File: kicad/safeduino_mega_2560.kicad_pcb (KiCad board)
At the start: 4 copper layers, 134.5 x 63.9 mm, 128 parts, among them X1 USB

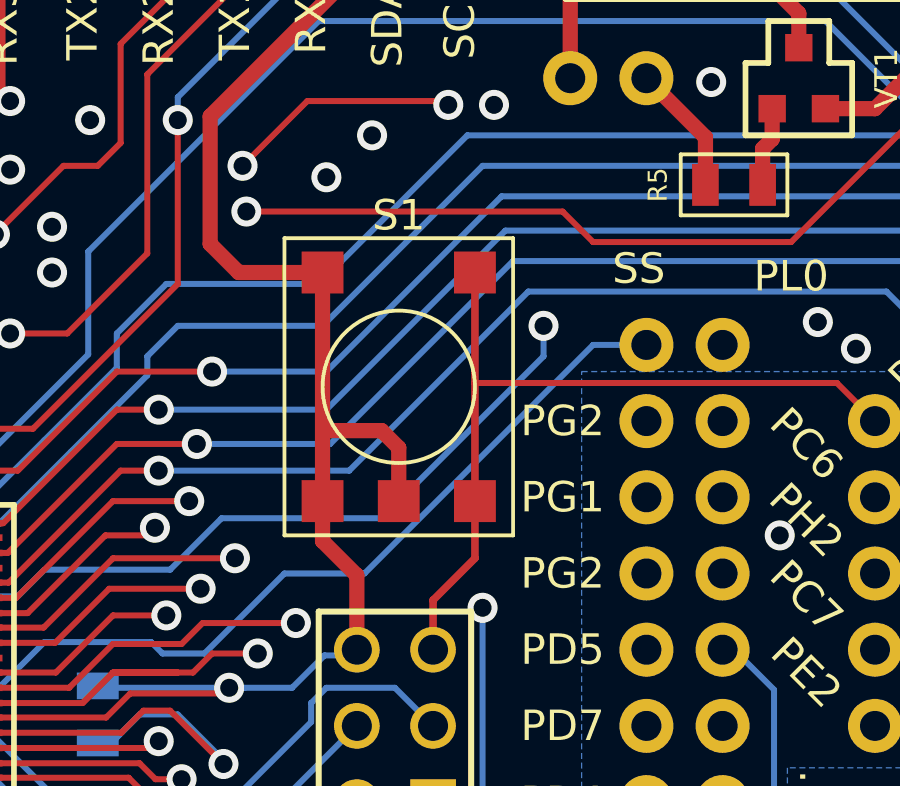
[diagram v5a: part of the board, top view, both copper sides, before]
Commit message: Поправил шелкографию и посадочное место для кнопки Reset.
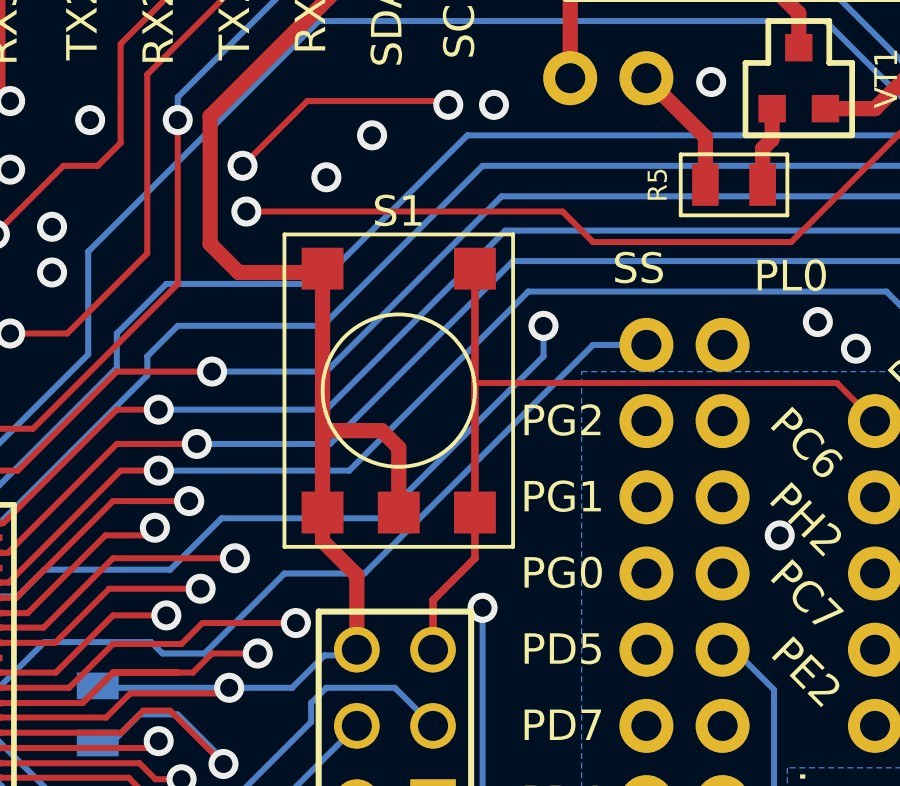
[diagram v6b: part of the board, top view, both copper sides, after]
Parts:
- moved S1 0.13 mm to (137.8, 114.3)
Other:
- board text added: "PG0"
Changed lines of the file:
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@@
     )
   )
-  (module SWD_BUTTON (layer Front)
-    (at 137.795 114.427 270)
-    (fp_text reference S1 (at -5.715 0 360) (layer F.SilkS)
-      (effects (font (size 1.016 1.016) (thickness 0.2032)))
-    )
-    (fp_text value DTSGL-61K (at 0.381 4.826 270) (layer F.SilkS) hide
-      (effects (font (size 1.016 1.016) (thickness 0.2032)))
-    )
-    (fp_line (start -4.953 3.81) (end 4.953 3.81) (layer F.SilkS) (width 0.127))
-    (fp_line (start -4.953 -3.81) (end 4.953 -3.81) (layer F.SilkS) (width 0.127))
-    (fp_circle (center 0 0) (end 0 -2.54) (layer F.SilkS) (width 0.127))
-    (fp_line (start 4.953 -3.81) (end 4.953 3.81) (layer F.SilkS) (width 0.127))
-    (fp_line (start -4.953 -3.81) (end -4.953 3.81) (layer F.SilkS) (width 0.127))
-    (pad 5 smd rect (at 3.81 0 270) (size 1.397 1.397)
-      (layers Front F.Paste F.Mask)
-      (net 21 /GND)
-    )
-    (pad 2 smd rect (at 3.81 -2.54 270) (size 1.397 1.397)
-      (layers Front F.Paste F.Mask)
-      (net 94 /RESET)
-    )
-    (pad 4 smd rect (at 3.81 2.54 270) (size 1.397 1.397)
-      (layers Front F.Paste F.Mask)
-      (net 21 /GND)
-    )
-    (pad 1 smd rect (at -3.81 -2.54 270) (size 1.397 1.397)
-      (layers Front F.Paste F.Mask)
-      (net 94 /RESET)
-    )
-    (pad 3 smd rect (at -3.81 2.54 270) (size 1.397 1.397)
-      (layers Front F.Paste F.Mask)
-      (net 21 /GND)
-    )
-  )
   (module CASE_C (layer Front)
     (at 75.692 124.206 180)
@@
     )
   )
+  (module SWD_BUTTON (layer Front)
+    (at 137.795 114.3 270)
+    (fp_text reference S1 (at -5.715 0 360) (layer F.SilkS)
+      (effects (font (size 1.016 1.016) (thickness 0.2032)))
+    )
+    (fp_text value DTSGL-61K (at 0.381 4.826 270) (layer F.SilkS) hide
+      (effects (font (size 1.016 1.016) (thickness 0.2032)))
+    )
+    (fp_line (start -4.953 3.81) (end 5.461 3.81) (layer F.SilkS) (width 0.127))
+    (fp_line (start -4.953 -3.81) (end 5.461 -3.81) (layer F.SilkS) (width 0.127))
+    (fp_circle (center 0.254 0) (end 0.254 -2.54) (layer F.SilkS) (width 0.127))
+    (fp_line (start 5.461 -3.81) (end 5.461 3.81) (layer F.SilkS) (width 0.127))
+    (fp_line (start -4.953 -3.81) (end -4.953 3.81) (layer F.SilkS) (width 0.127))
+    (pad 5 smd rect (at 4.318 0 270) (size 1.397 1.397)
+      (layers Front F.Paste F.Mask)
+      (net 21 /GND)
+    )
+    (pad 2 smd rect (at 4.318 -2.54 270) (size 1.397 1.397)
+      (layers Front F.Paste F.Mask)
+      (net 94 /RESET)
+    )
+    (pad 4 smd rect (at 4.318 2.54 270) (size 1.397 1.397)
+      (layers Front F.Paste F.Mask)
+      (net 21 /GND)
+    )
+    (pad 1 smd rect (at -3.81 -2.54 270) (size 1.397 1.397)
+      (layers Front F.Paste F.Mask)
+      (net 94 /RESET)
+    )
+    (pad 3 smd rect (at -3.81 2.54 270) (size 1.397 1.397)
+      (layers Front F.Paste F.Mask)
+      (net 21 /GND)
+    )
+  )
   (gr_text GND (at 155.448 151.765) (layer F.SilkS)
     (effects (font (size 1.016 1.016) (thickness 0.127)))
@@
     (effects (font (size 1.016 1.016) (thickness 0.127)))
   )
-  (gr_text PG2 (at 143.256 120.65) (layer F.SilkS)
+  (gr_text PG0 (at 143.256 120.65) (layer F.SilkS)
     (effects (font (size 1.016 1.016) (thickness 0.127)))
   )

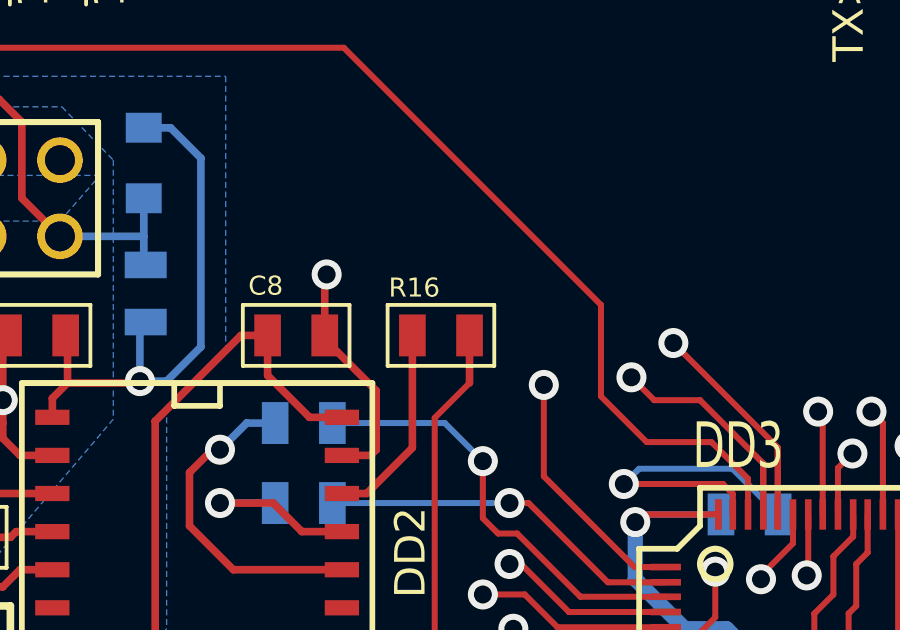
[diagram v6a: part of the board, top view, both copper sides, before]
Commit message: Заменил резистор R16 на диод для защиты ADUM от попадания напряжения на входную ногу.
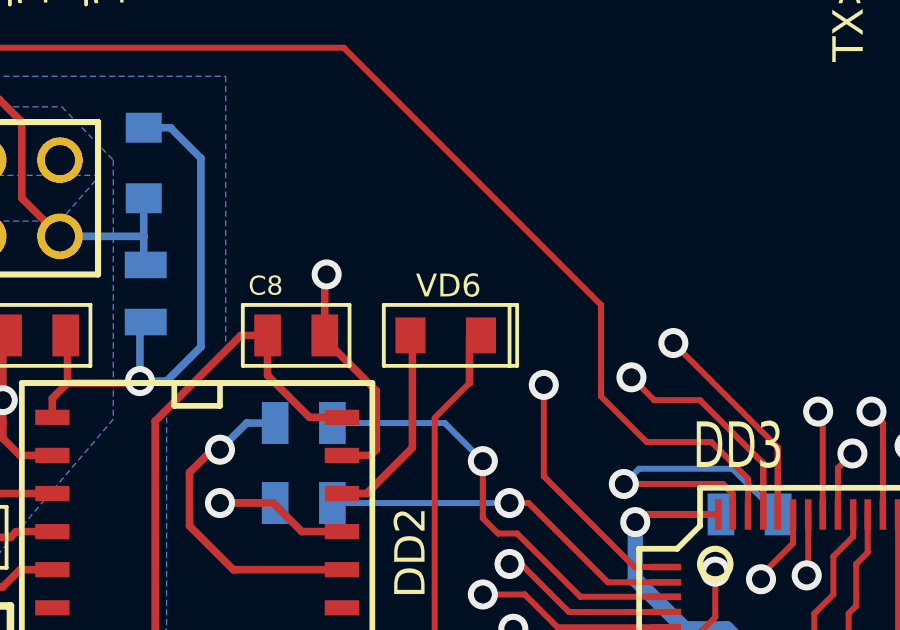
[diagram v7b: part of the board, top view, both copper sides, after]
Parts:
- removed R16: 0, SMD0805
- added VD6: BAS216, SOD110, F.Cu at (100.1, 111.3)

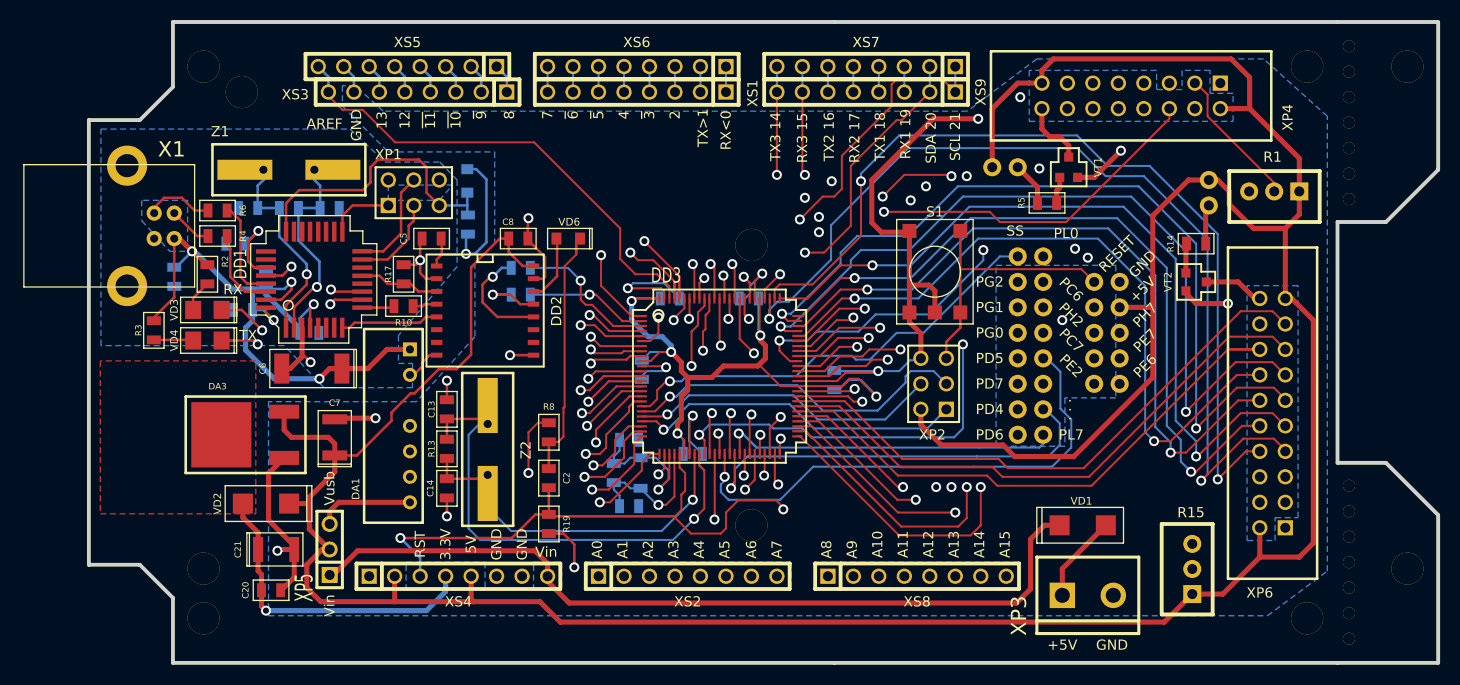
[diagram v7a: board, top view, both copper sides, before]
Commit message: Приступил к разработке новой ревизии платы SafeDuino MEGA 2560 ver. 1.1.
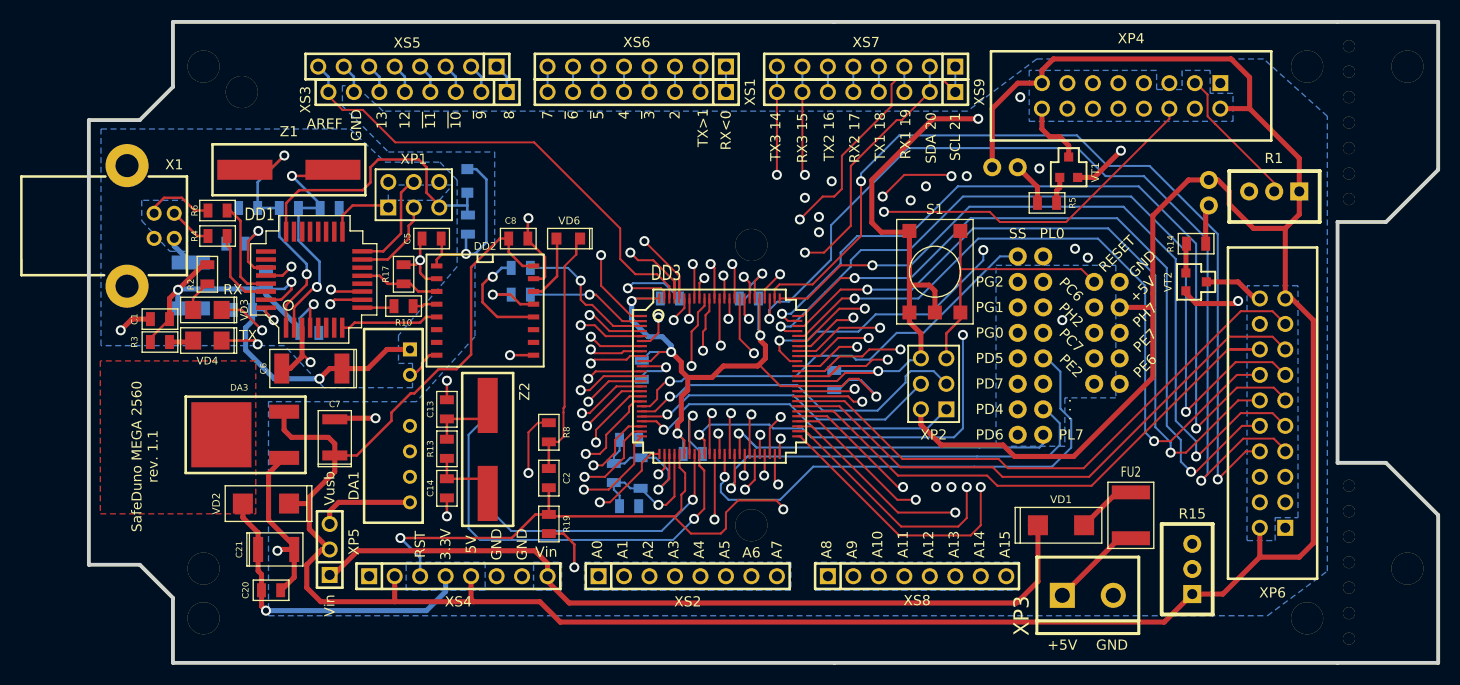
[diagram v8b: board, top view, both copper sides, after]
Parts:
- added FU1: MF-MSMF050, IWsmd_case:SMD1812, B.Cu at (63.6, 115.9)
- added FU2: MF-MSMF050, IWsmd_case:SMD1812, F.Cu at (157.3, 138.8)
- C1: footprint SMD0805 -> IWsmd_case:SMD0805; moved to F.Cu
- C10, C11, C12, C13, C14, C15, C16, C17, C18, C19, C2, C20, C22, C23, C3, C4, C5, C8, C9, R10, R11, R12, R13, R14, R17, R18, R19, R2, R3, R4, R5, R6, R7, R8, R9: footprint SMD0805 -> IWsmd_case:SMD0805
- C21, C7: footprint CASE_B -> IWsmd_case:CASE_B
- C6: footprint CASE_C -> IWsmd_case:CASE_C
- DA1: footprint P10LU-0515ZLF -> IWcomponents:P10LU-0515ZLF
- DA3: footprint TO_252 -> IWsmd_case:TO_252
- DD1: footprint TQFP32_case -> IWsmd_case:TQFP32_case
- DD2: value ADUM1301 -> ADUM1301BRWZ; footprint SOIC16_RW16 -> IWsmd_case:SOIC16_RW16
- DD3: footprint TQFP100_case -> IWsmd_case:TQFP100_case
- R1, R15: footprint Electron_3296W -> IWcomponents:Electron_3296W
- S1: footprint SWD_BUTTON -> IWsmd_case:SWD_BUTTON
- VD1, VD2: footprint SMA -> IWcomponents:SMA
- VD3, VD4: footprint LED1206 -> IWsmd_case:LED1206
- VD5, VD6: footprint SOD110 -> IWcomponents:SOD110
- VT1, VT2: footprint SOT_23 -> IWcomponents:SOT_23
- X1: footprint USB_B -> IWconnectors:CONN_USB-B
- XP1, XP2: footprint pin_array_3x2 -> IWconnectors:PIN_ARRAY_3x2
- XP3: footprint AWG12-2 -> IWconnectors:DG126-5.0-02P-14
- XP4: footprint IDC-16MS -> IWconnectors:IDC-16MS
- XP5: footprint SIL-3 -> IWconnectors:PIN_ARRAY_3x1
- XP6: footprint IDC-20MS -> IWconnectors:IDC-20MS
- XS1, XS2, XS3, XS4, XS5, XS6, XS7, XS8, XS9: footprint PIN_ARRAY_8x1 -> IWconnectors:PIN_ARRAY_8x1
- Z1, Z2: footprint Q_49U3HMS& -> IWcomponents:HC-49SM
- Z3: footprint SMD0301M2-2 -> IWsmd_case:SMD0301M2-2
- moved C1 4.45 mm to (60.6, 119.3), turned to 180 degrees
- moved X1 2.92 mm to (54.4, 110.0), turned to 90 degrees
- moved XP6 2.54 mm to (171.4, 128.7)
- moved VD1 2.16 mm to (150.4, 139.8)
- moved R3 1.32 mm to (60.6, 121.6), turned to 180 degrees
- moved XP2 1.27 mm to (136.4, 125.7)
- moved XP1 1.07 mm to (85.9, 105.6)
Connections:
- DD1 pad 12: (no net) -> Net-(DD1-Pad12)
- DD1 pad 14: (no net) -> Net-(DD1-Pad14)
- DD1 pad 18: (no net) -> Net-(DD1-Pad18)
- DD1 pad 19: (no net) -> Net-(DD1-Pad19)
- DD1 pad 20: (no net) -> Net-(DD1-Pad20)
- DD1 pad 21: (no net) -> Net-(DD1-Pad21)
- DD1 pad 22: (no net) -> Net-(DD1-Pad22)
- DD1 pad 23: (no net) -> Net-(DD1-Pad23)
- DD1 pad 25: (no net) -> Net-(DD1-Pad25)
- DD1 pad 26: (no net) -> Net-(DD1-Pad26)
- DD1 pad 5: (no net) -> Net-(DD1-Pad5)
- DD1 pad 6: (no net) -> Net-(DD1-Pad6)
- DD1 pad 7: (no net) -> Net-(DD1-Pad7)
- DD2 pad 10: (no net) -> Net-(DD2-Pad10)
- DD2 pad 7: (no net) -> Net-(DD2-Pad7)
- VD1 pad 1: N-00000105 -> Net-(FU2-Pad2)
- X1 pad 1: /5V_USB -> Net-(FU1-Pad1)
- X1 pad 5: (no net) -> Net-(X1-Pad5)
- X1 pad 6: (no net) -> Net-(X1-Pad6)
- XP3 pad 1: N-00000105 -> Net-(FU2-Pad1)
- XP4 pad 10: (no net) -> Net-(XP4-Pad10)
- XP4 pad 7: (no net) -> Net-(XP4-Pad7)
- XP4 pad 8: (no net) -> Net-(XP4-Pad8)
- XP4 pad 9: (no net) -> Net-(XP4-Pad9)
- XS4 pad 1: (no net) -> Net-(XS4-Pad1)
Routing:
- net Net-(FU2-Pad1): track 0.00 -> 9.44 mm
- net N-00000105: track 8.78 -> 0.00 mm
- net Net-(FU2-Pad2): track 0.00 -> 6.02 mm
- net Net-(C3-Pad1): track 20.1 -> 25.1 mm, vias 1 -> 2
- net Net-(FU1-Pad1): track 0.00 -> 4.10 mm
- net /GND_USB: track 23.0 -> 26.5 mm, vias 3 -> 4
- net /5V_USB: track 120.6 -> 117.3 mm
- net Net-(C4-Pad1): track 20.2 -> 23.0 mm, vias 1 -> 2
- net Net-(R3-Pad1): track 3.94 -> 2.65 mm
- net /GND: track 148.0 -> 149.2 mm
- net /VCCIN: track 83.1 -> 82.4 mm
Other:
- board text added: "SafeDuno MEGA 2560 rev. 1.1"
